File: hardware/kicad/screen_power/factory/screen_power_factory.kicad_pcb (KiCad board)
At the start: 4 copper layers, 130 x 120 mm, 72 parts, among them J1 AUX 5V INPUT, J101 PI USB, J102 TOUCH, J103 SCREEN POWER 5V 3A, J2 SCREEN CONTROL, J201 PI USB, J202 TOUCH, J203 SCREEN POWER 5V 3A, Q1 MMBT3904,215, Q101 2N7002, Q102 2N7002, Q201 2N7002, Q202 2N7002, U101 ADuM3165BRSZ, U102 SN74LVC1G14DBVR, U103 TPS25221DBVR, U104 TPS25810RVCR, U201 ADuM3165BRSZ, U202 SN74LVC1G14DBVR, U203 TPS25221DBVR, U204 TPS25810RVCR, Y101 24MHz 10pF, Y201 24MHz 10pF

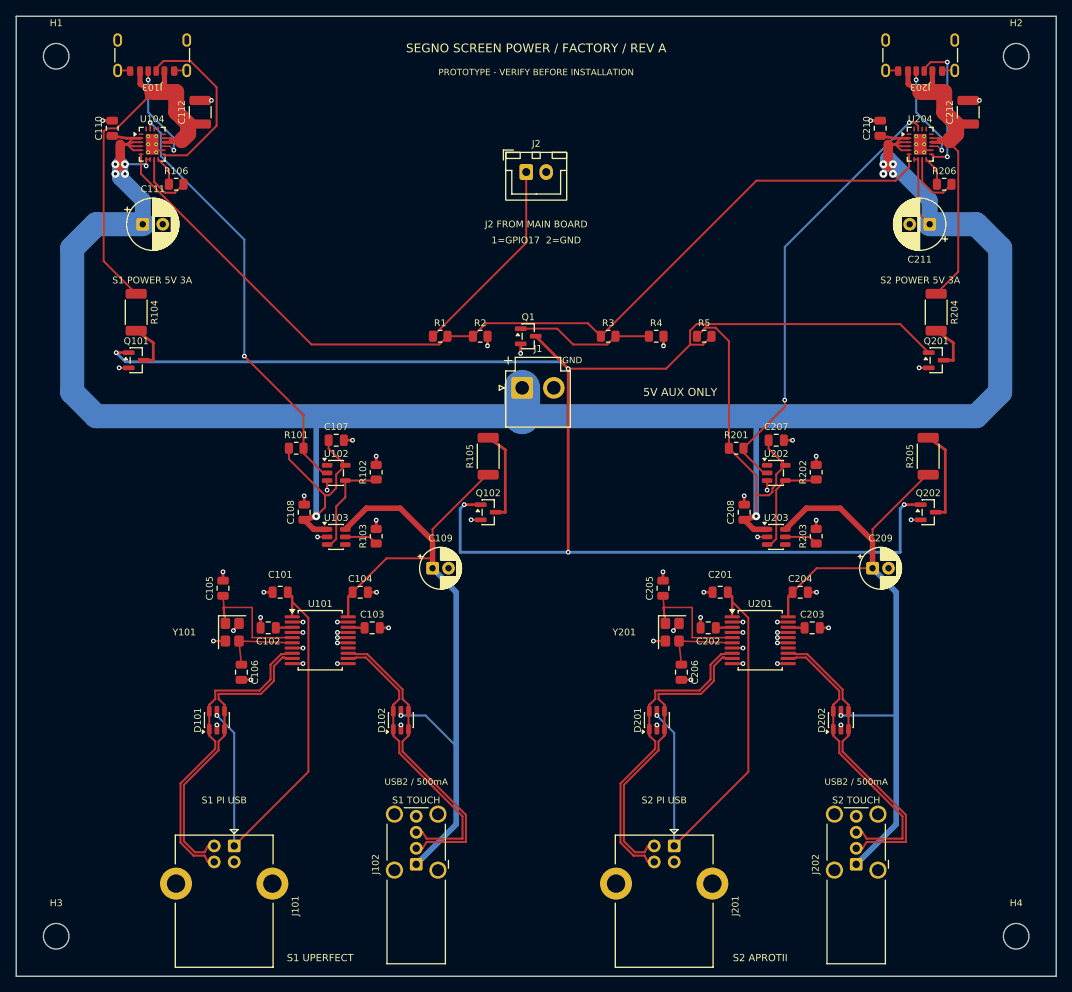
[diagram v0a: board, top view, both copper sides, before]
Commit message: refactor(hardware): simplify and compact screen power boards
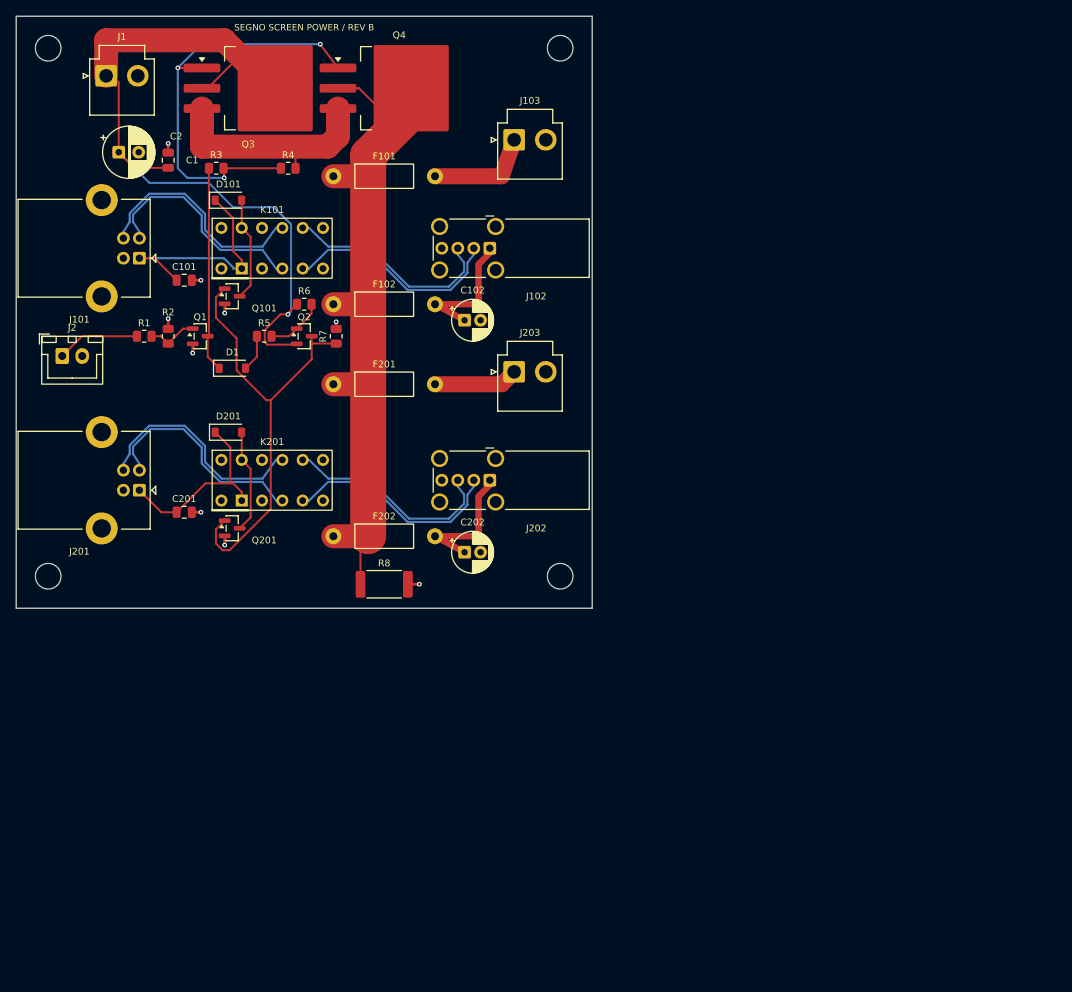
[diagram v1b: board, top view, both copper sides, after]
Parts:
- removed C103, C104, C107, C108, C110, C203, C204, C207, C208, C210: 100nF, C_0805_2012Metric
- removed C105, C106, C205, C206: 8pF C0G, C_0805_2012Metric
- removed C109, C209: 150uF 10V, CP_Radial_D5.0mm_P2.00mm
- removed C111, C211: 220uF 10V, CP_Radial_D6.3mm_P2.50mm
- removed C112, C212: 10uF 25V X7R, C_1210_3225Metric
- removed D102, D202: USBLC6-2SC6, SOT-23-6
- removed Q102, Q202: 2N7002, SOT-23
- removed R101, R102, R201, R202: 10k, R_0805_2012Metric
- removed R103, R203: 80.6k 1%, R_0805_2012Metric
- removed R104, R105, R204, R205: 100R 0.75W, R_2010_5025Metric
- removed R106, R206: 100k 1%, R_0805_2012Metric
- removed U101, U201: ADuM3165BRSZ, SSOP-20_5.3x7.2mm_P0.65mm
- removed U102, U202: SN74LVC1G14DBVR, SOT-23-5
- removed U103, U203: TPS25221DBVR, SOT-23-6
- removed U104, U204: TPS25810RVCR, Texas_RVC0020A_WQFN-20-1EP_3x4mm_P0.5mm_EP1.6x2.6mm_ThermalVias
- removed Y101, Y201: 24MHz 10pF, Crystal_SMD_3225-4Pin_3.2x2.5mm
- added C1: 100nF 50V, C_0805_2012Metric, F.Cu at (19.0, 18.0)
- added C2: 220uF 10V, CP_Radial_D6.3mm_P2.50mm, F.Cu at (12.8, 17.0)
- added D1: 1N4148W, D_SOD-123, F.Cu at (27.0, 44.0)
- added F101: 4A fast, Fuse_Littelfuse_251_P12.70mm, F.Cu at (39.6, 20.0)
- added F102: 750mA fast, Fuse_Littelfuse_251_P12.70mm, F.Cu at (39.6, 36.0)
- added F201: 4A fast, Fuse_Littelfuse_251_P12.70mm, F.Cu at (39.6, 46.0)
- added F202: 750mA fast, Fuse_Littelfuse_251_P12.70mm, F.Cu at (39.6, 65.0)
- added K101: G6K-2P-RF DC5, Relay_DPDT_Omron_G6K-2P-RF, F.Cu at (32.0, 29.0)
- added K201: G6K-2P-RF DC5, Relay_DPDT_Omron_G6K-2P-RF, F.Cu at (32.0, 58.0)
- added Q2: MMBT3906, SOT-23, F.Cu at (36.0, 40.0)
- added Q3: SUM70101EL, TO-263-3_TabPin2, F.Cu at (30.9, 9.00)
- added Q4: SUM70101EL, TO-263-3_TabPin2, F.Cu at (47.9, 9.00)
- added R6: 100k 1%, R_0805_2012Metric, F.Cu at (36.0, 36.0)
- added R7: 100k 1%, R_0805_2012Metric, F.Cu at (40.0, 40.0)
- added R8: 100R 1W 1%, R_2512_6332Metric, F.Cu at (46.0, 71.0)
- C101, C201: value 100nF -> 100nF 50V
- C102, C202: value 100nF -> 150uF 10V; footprint C_0805_2012Metric -> CP_Radial_D5.0mm_P2.00mm
- D101, D201: value USBLC6-2SC6 -> 1N4148W; footprint SOT-23-6 -> D_SOD-123
- J103: value SCREEN POWER 5V 3A -> SCREEN 1 POWER; footprint USB_C_Receptacle_GCT_USB4125-xx-x_6P_TopMnt_Horizontal -> JST_VH_B2P-VH_1x02_P3.96mm_Vertical
- J2: value SCREEN CONTROL -> GPIO17 / GND
- J203: value SCREEN POWER 5V 3A -> SCREEN 2 POWER; footprint USB_C_Receptacle_GCT_USB4125-xx-x_6P_TopMnt_Horizontal -> JST_VH_B2P-VH_1x02_P3.96mm_Vertical
- Q1: value MMBT3904,215 -> MMBT3904
- R1: value 1k -> 1k 1%
- R2: value 10k -> 100k 1%
- R3: value 10k -> 4.7k 1%
- R4: value 100k -> 330k 1%
- R5: value 10k -> 5.6k 1%
- moved Q201 90.5 mm to (27.0, 64.0)
- moved J201 80.3 mm to (15.4, 59.2), turned to 180 degrees
- moved J102 77.6 mm to (59.2, 29.0), turned to 180 degrees
- moved J101 74.4 mm to (15.4, 30.2), turned to 180 degrees
- moved H4 72.6 mm to (68.0, 70.0)
- moved C201 67.7 mm to (21.0, 62.0), turned to 0 degrees
- moved J202 66.4 mm to (59.2, 58.0), turned to 180 degrees
- moved J203 65.0 mm to (62.2, 44.5), turned to 0 degrees
- moved D101 65.0 mm to (26.5, 23.0), turned to 0 degrees
- moved J1 65.0 mm to (11.2, 7.45)
- moved D201 64.5 mm to (26.5, 52.0), turned to 0 degrees
- moved J2 62.4 mm to (5.75, 42.5)
- moved H2 57.0 mm to (68.0, 4.00)
- moved R5 55.0 mm to (31.0, 40.0)
- moved R3 53.3 mm to (25.0, 19.0)
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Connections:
- C102 pad 1: S1_VDD1 -> S1_TOUCH_5V
- C202 pad 1: S2_VDD1 -> S2_TOUCH_5V
- D101 pad 1: S1_UP_P -> HOST1_5V
- D101 pad 2: GND -> S1_DATA_COIL_LOW
- D201 pad 1: S2_UP_P -> HOST2_5V
- D201 pad 2: GND -> S2_DATA_COIL_LOW
- Q1 pad 1: DUMP_BASE -> CONTROL_BASE
- Q1 pad 3: DISCHARGE -> CONTROL_SINK
- Q101 pad 1: DISCHARGE -> DATA_ENABLE
- Q101 pad 3: S1_DUMP0 -> S1_DATA_COIL_LOW
- Q201 pad 1: DISCHARGE -> DATA_ENABLE
- Q201 pad 3: S2_DUMP0 -> S2_DATA_COIL_LOW
- R1 pad 2: DISPLAY_ENABLE -> CONTROL_BASE
- R2 pad 1: DISPLAY_ENABLE -> CONTROL_BASE
- R3 pad 1: DISPLAY_ENABLE -> CONTROL_SINK
- R3 pad 2: DUMP_BASE -> POWER_GATE
- R4 pad 1: DUMP_BASE -> POWER_GATE
- R4 pad 2: GND -> COMMON_SOURCE
- R5 pad 1: AUX_5V -> BUFFER_SINK
- R5 pad 2: DISCHARGE -> BUFFER_BASE
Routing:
- net AUX_5V: track 347.9 -> 100.2 mm, vias 11 -> 1
- net DISCHARGE: track 212.0 -> 0.00 mm, vias 5 -> 0
- net DISPLAY_ENABLE: track 119.4 -> 0.00 mm
- net SWITCHED_5V: track 0.00 -> 89.8 mm
- net S1_TOUCH_5V: track 92.7 -> 16.9 mm, vias 1 -> 0
- net S2_TOUCH_5V: track 90.8 -> 16.9 mm, vias 1 -> 0
- net GND: track 83.5 -> 10.5 mm, vias 61 -> 9
- net DATA_ENABLE: track 0.00 -> 57.0 mm
- net S2_UFP_N: track 55.5 -> 0.00 mm, vias 2 -> 0
- net S1_UFP_N: track 54.1 -> 0.00 mm, vias 2 -> 0
- net POWER_GATE: track 0.00 -> 53.1 mm, vias 0 -> 3
- net S1_MAIN_5V: track 58.2 -> 13.1 mm
- net S2_MAIN_5V: track 48.7 -> 10.5 mm
- net HOST2_5V: track 56.3 -> 24.1 mm, vias 1 -> 0
- net COMMON_SOURCE: track 0.00 -> 28.9 mm
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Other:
- board size 130 x 120 mm -> 72 x 74 mm
- board text added: "1=5V 2=GND"
- board text added: "4L / GND L2 L3"
- board text added: "5V IN"
- board text added: "GPIO17 / GND"
- board text added: "S1 5V OUT"
- board text added: "S1 PI"
- board text added: "S2 5V OUT"
- board text added: "S2 PI"
- board text added: "SEGNO SCREEN POWER / REV B"
- board text added: "USB 90 OHM"
- board text removed: "+"
- board text removed: "1=GPIO17 2=GND"
- board text removed: "4 LAYERS / 1.6mm / JLC04161H-7628"
- board text removed: "5V AUX ONLY"
- board text removed: "F + B SIGNAL / INNER 1 + 2 GROUND"
- board text removed: "FABRICATOR: CONFIRM 90 OHM DIFFERENTIAL"
- board text removed: "GND"
- board text removed: "J2 FROM MAIN BOARD"
- board text removed: "PROTOTYPE - VERIFY BEFORE INSTALLATION"
- board text removed: "S1 PI USB"
- board text removed: "S1 POWER 5V 3A"
- board text removed: "S1 UPERFECT"
- board text removed: "S2 APROTII"
- board text removed: "S2 PI USB"
- board text removed: "S2 POWER 5V 3A"
- board text removed: "SEGNO SCREEN POWER / FACTORY / REV A"
- board text removed: "USB PAIRS: 0.26mm WIDTH / 0.16mm GAP"
- board text removed: "USB2 / 500mA"
